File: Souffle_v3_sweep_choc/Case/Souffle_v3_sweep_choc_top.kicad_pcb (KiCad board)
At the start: 2 copper layers, 132.1 x 108 mm, 5 parts

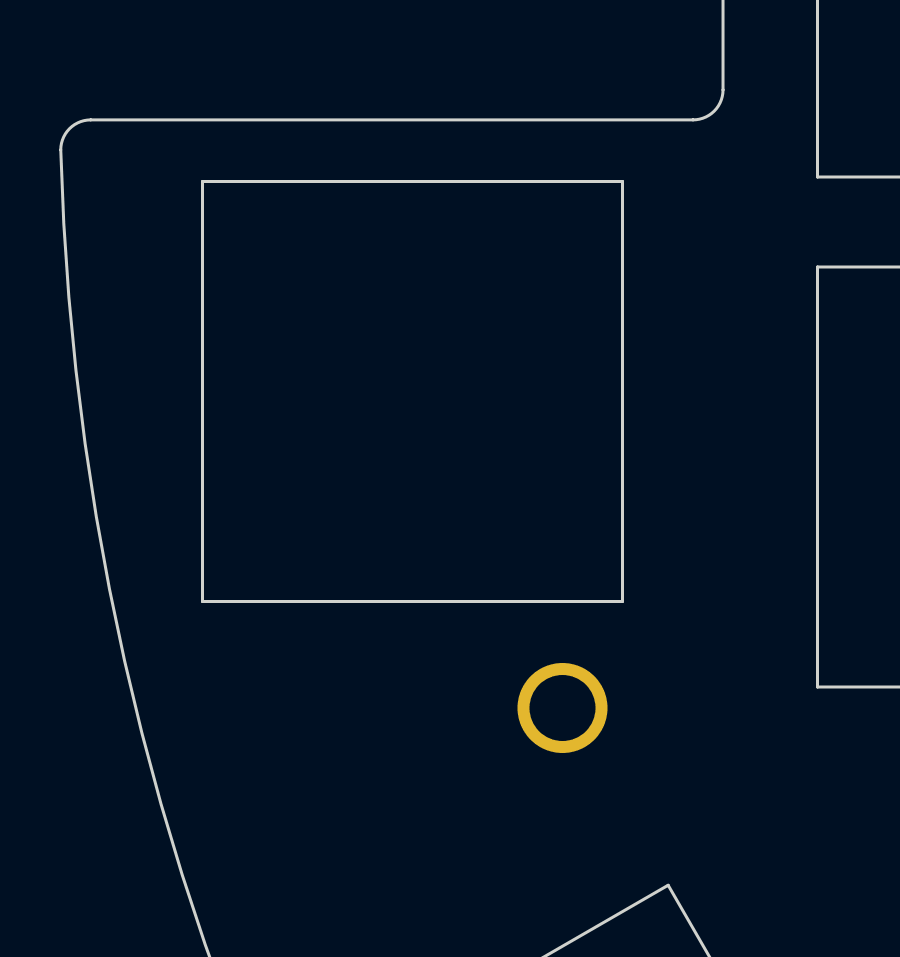
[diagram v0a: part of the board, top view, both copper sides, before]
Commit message: Fixed horizontal spacing of the FN key.
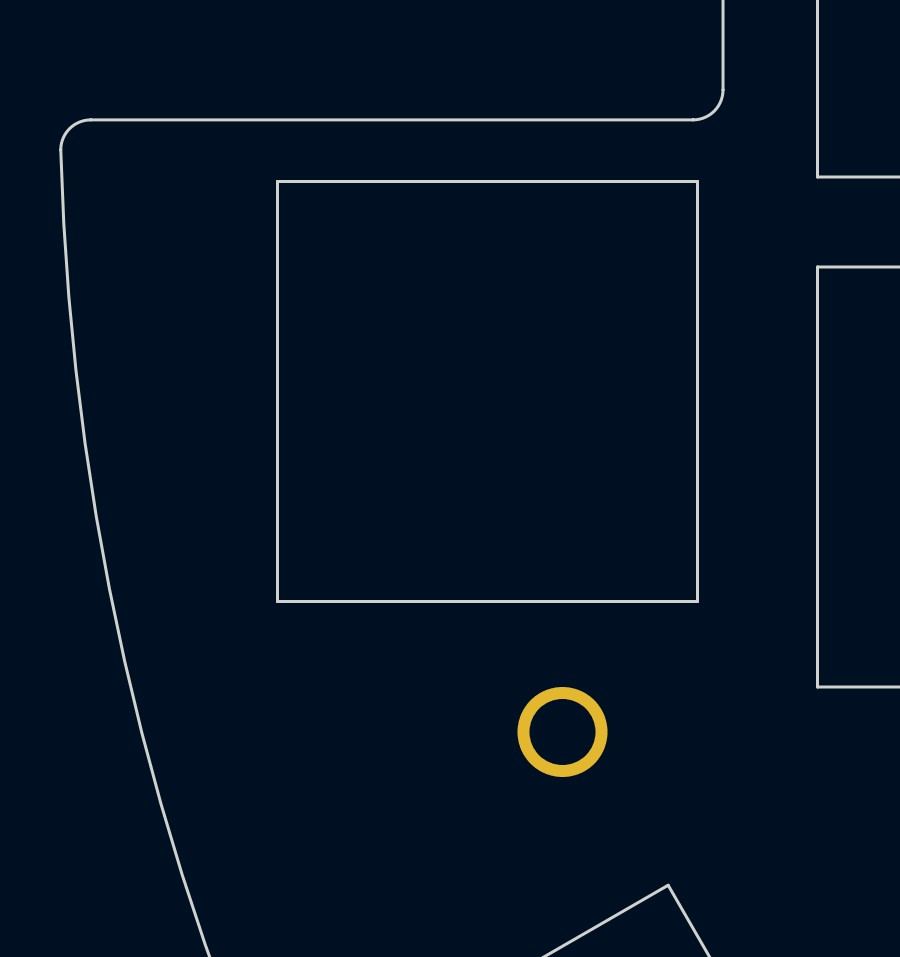
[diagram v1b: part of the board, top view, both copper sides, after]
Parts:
- moved TH2 0.80 mm to (90.6, 111.1)
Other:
- outline, holes or cut-outs redrawn
